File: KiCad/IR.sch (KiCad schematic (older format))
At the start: 30 parts, among them IC2 ATTINY85-P, IC3 ATTINY85-P, Q2 Q_NPN_BCE, Q3 Q_NPN_BCE

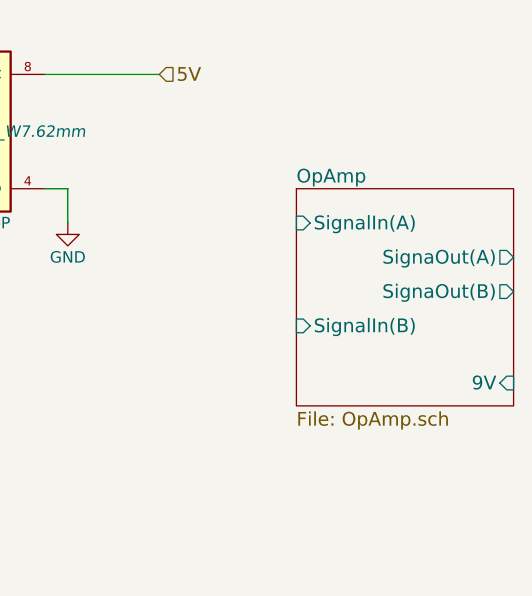
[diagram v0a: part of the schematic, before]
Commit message: Updated the schematics and started with the PCB
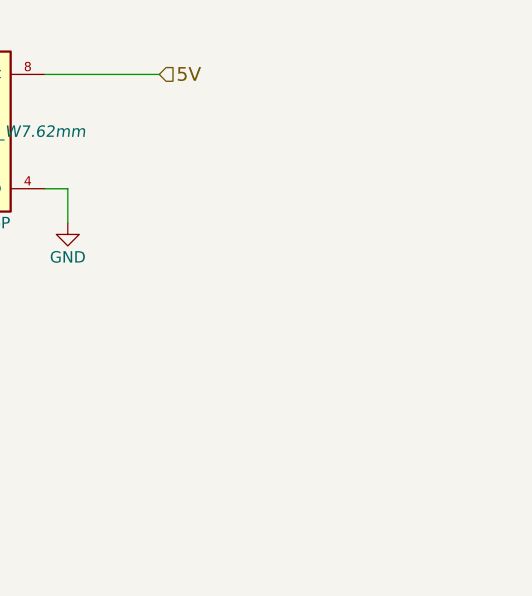
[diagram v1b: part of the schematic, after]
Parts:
- D1, D10, D11, D12, D2, D3, D4, D5, D6, D7, D8, D9: footprint LEDs:LED-5MM -> Wire_Connections_Bridges:WireConnection_1.50mmDrill
- R10, R11, R12, R13, R14, R15, R16, R17, R18, R19, R20, R21, R8, R9: footprint Resistors_ThroughHole:Resistor_Horizontal_RM20mm -> Resistors_ThroughHole:Resistor_Vertical_RM5mm
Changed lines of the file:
@@
 $Descr A4 11693 8268
 encoding utf-8
-Sheet 3 7
+Sheet 3 6
 Title ""
 Date ""
@@
 SCL
 $Comp
-L GND #PWR013
+L GND #PWR016
 U 1 1 57175BA8
 P 8550 2050
-F 0 "#PWR013" H 8550 1800 50  0001 C CNN
+F 0 "#PWR016" H 8550 1800 50  0001 C CNN
 F 1 "GND" H 8550 1900 50  0000 C CNN
 F 2 "" H 8550 2050 50  0000 C CNN
@@
 F 0 "D9" H 3200 3250 50  0000 C CNN
 F 1 "IR_Recieve" H 3216 2983 50  0000 C CNN
-F 2 "LEDs:LED-5MM" H 3200 3150 50  0001 C CNN
+F 2 "Wire_Connections_Bridges:WireConnection_1.50mmDrill" H 3200 3150 50  0001 C CNN
 F 3 "" H 3200 3150 50  0000 C CNN
 	1    3200 3150
@@
 F 0 "D7" H 2800 3250 50  0000 C CNN
 F 1 "LED" V 2800 3050 50  0000 C CNN
-F 2 "LEDs:LED-5MM" H 2800 3150 50  0001 C CNN
+F 2 "Wire_Connections_Bridges:WireConnection_1.50mmDrill" H 2800 3150 50  0001 C CNN
 F 3 "" H 2800 3150 50  0000 C CNN
 	1    2800 3150
@@
 F 0 "D11" H 3600 3250 50  0000 C CNN
 F 1 "LED" V 3600 3050 50  0000 C CNN
-F 2 "LEDs:LED-5MM" H 3600 3150 50  0001 C CNN
+F 2 "Wire_Connections_Bridges:WireConnection_1.50mmDrill" H 3600 3150 50  0001 C CNN
 F 3 "" H 3600 3150 50  0000 C CNN
 	1    3600 3150
@@
 F 0 "R16" V 3280 2600 50  0000 C CNN
 F 1 "100" V 3200 2600 50  0000 C CNN
-F 2 "Resistors_ThroughHole:Resistor_Horizontal_RM20mm" V 3130 2600 50  0001 C CNN
+F 2 "Resistors_ThroughHole:Resistor_Vertical_RM5mm" V 3130 2600 50  0001 C CNN
 F 3 "" H 3200 2600 50  0000 C CNN
 	1    3200 2600
@@
 F 0 "R18" V 3680 2600 50  0000 C CNN
 F 1 "22" V 3600 2600 50  0000 C CNN
-F 2 "Resistors_ThroughHole:Resistor_Horizontal_RM20mm" V 3530 2600 50  0001 C CNN
+F 2 "Resistors_ThroughHole:Resistor_Vertical_RM5mm" V 3530 2600 50  0001 C CNN
 F 3 "" H 3600 2600 50  0000 C CNN
 	1    3600 2600
@@
 F 0 "R14" V 2880 2600 50  0000 C CNN
 F 1 "22" V 2800 2600 50  0000 C CNN
-F 2 "Resistors_ThroughHole:Resistor_Horizontal_RM20mm" V 2730 2600 50  0001 C CNN
+F 2 "Resistors_ThroughHole:Resistor_Vertical_RM5mm" V 2730 2600 50  0001 C CNN
 F 3 "" H 2800 2600 50  0000 C CNN
 	1    2800 2600
@@
 F 0 "D3" H 1700 3250 50  0000 C CNN
 F 1 "IR_Recieve" H 1716 2983 50  0000 C CNN
-F 2 "LEDs:LED-5MM" H 1700 3150 50  0001 C CNN
+F 2 "Wire_Connections_Bridges:WireConnection_1.50mmDrill" H 1700 3150 50  0001 C CNN
 F 3 "" H 1700 3150 50  0000 C CNN
 	1    1700 3150
@@
 F 0 "D1" H 1300 3250 50  0000 C CNN
 F 1 "LED" V 1300 3050 50  0000 C CNN
-F 2 "LEDs:LED-5MM" H 1300 3150 50  0001 C CNN
+F 2 "Wire_Connections_Bridges:WireConnection_1.50mmDrill" H 1300 3150 50  0001 C CNN
 F 3 "" H 1300 3150 50  0000 C CNN
 	1    1300 3150
@@
 F 0 "D5" H 2100 3250 50  0000 C CNN
 F 1 "LED" V 2100 3050 50  0000 C CNN
-F 2 "LEDs:LED-5MM" H 2100 3150 50  0001 C CNN
+F 2 "Wire_Connections_Bridges:WireConnection_1.50mmDrill" H 2100 3150 50  0001 C CNN
 F 3 "" H 2100 3150 50  0000 C CNN
 	1    2100 3150
@@
 F 0 "R10" V 1780 2600 50  0000 C CNN
 F 1 "100" V 1700 2600 50  0000 C CNN
-F 2 "Resistors_ThroughHole:Resistor_Horizontal_RM20mm" V 1630 2600 50  0001 C CNN
+F 2 "Resistors_ThroughHole:Resistor_Vertical_RM5mm" V 1630 2600 50  0001 C CNN
 F 3 "" H 1700 2600 50  0000 C CNN
 	1    1700 2600
@@
 $EndComp
 $Comp
-L GND #PWR014
+L GND #PWR017
 U 1 1 57175C1F
 P 3900 3750
-F 0 "#PWR014" H 3900 3500 50  0001 C CNN
+F 0 "#PWR017" H 3900 3500 50  0001 C CNN
 F 1 "GND" H 3900 3600 50  0000 C CNN
 F 2 "" H 3900 3750 50  0000 C CNN
@@
 F 0 "R20" V 3880 4050 50  0000 C CNN
 F 1 "1K" V 3800 4050 50  0000 C CNN
-F 2 "Resistors_ThroughHole:Resistor_Horizontal_RM20mm" V 3730 4050 50  0001 C CNN
+F 2 "Resistors_ThroughHole:Resistor_Vertical_RM5mm" V 3730 4050 50  0001 C CNN
 F 3 "" H 3800 4050 50  0000 C CNN
 	1    3800 4050
@@
 F 0 "R12" V 2180 2600 50  0000 C CNN
 F 1 "22" V 2100 2600 50  0000 C CNN
-F 2 "Resistors_ThroughHole:Resistor_Horizontal_RM20mm" V 2030 2600 50  0001 C CNN
+F 2 "Resistors_ThroughHole:Resistor_Vertical_RM5mm" V 2030 2600 50  0001 C CNN
 F 3 "" H 2100 2600 50  0000 C CNN
 	1    2100 2600
@@
 F 0 "R8" V 1380 2600 50  0000 C CNN
 F 1 "22" V 1300 2600 50  0000 C CNN
-F 2 "Resistors_ThroughHole:Resistor_Horizontal_RM20mm" V 1230 2600 50  0001 C CNN
+F 2 "Resistors_ThroughHole:Resistor_Vertical_RM5mm" V 1230 2600 50  0001 C CNN
 F 3 "" H 1300 2600 50  0000 C CNN
 	1    1300 2600
@@
 SCL
 $Comp
-L GND #PWR015
+L GND #PWR018
 U 1 1 5718B310
 P 8550 5100
-F 0 "#PWR015" H 8550 4850 50  0001 C CNN
+F 0 "#PWR018" H 8550 4850 50  0001 C CNN
 F 1 "GND" H 8550 4950 50  0000 C CNN
 F 2 "" H 8550 5100 50  0000 C CNN
@@
 F 0 "D10" H 3200 6300 50  0000 C CNN
 F 1 "IR_Recieve" H 3216 6033 50  0000 C CNN
-F 2 "LEDs:LED-5MM" H 3200 6200 50  0001 C CNN
+F 2 "Wire_Connections_Bridges:WireConnection_1.50mmDrill" H 3200 6200 50  0001 C CNN
 F 3 "" H 3200 6200 50  0000 C CNN
 	1    3200 6200
@@
 F 0 "D8" H 2800 6300 50  0000 C CNN
 F 1 "LED" V 2800 6100 50  0000 C CNN
-F 2 "LEDs:LED-5MM" H 2800 6200 50  0001 C CNN
+F 2 "Wire_Connections_Bridges:WireConnection_1.50mmDrill" H 2800 6200 50  0001 C CNN
 F 3 "" H 2800 6200 50  0000 C CNN
 	1    2800 6200
@@
 F 0 "D12" H 3600 6300 50  0000 C CNN
 F 1 "LED" V 3600 6100 50  0000 C CNN
-F 2 "LEDs:LED-5MM" H 3600 6200 50  0001 C CNN
+F 2 "Wire_Connections_Bridges:WireConnection_1.50mmDrill" H 3600 6200 50  0001 C CNN
 F 3 "" H 3600 6200 50  0000 C CNN
 	1    3600 6200
@@
 F 0 "R17" V 3280 5650 50  0000 C CNN
 F 1 "100" V 3200 5650 50  0000 C CNN
-F 2 "Resistors_ThroughHole:Resistor_Horizontal_RM20mm" V 3130 5650 50  0001 C CNN
+F 2 "Resistors_ThroughHole:Resistor_Vertical_RM5mm" V 3130 5650 50  0001 C CNN
 F 3 "" H 3200 5650 50  0000 C CNN
 	1    3200 5650
@@
 F 0 "R19" V 3680 5650 50  0000 C CNN
 F 1 "22" V 3600 5650 50  0000 C CNN
-F 2 "Resistors_ThroughHole:Resistor_Horizontal_RM20mm" V 3530 5650 50  0001 C CNN
+F 2 "Resistors_ThroughHole:Resistor_Vertical_RM5mm" V 3530 5650 50  0001 C CNN
 F 3 "" H 3600 5650 50  0000 C CNN
 	1    3600 5650
@@
 F 0 "R15" V 2880 5650 50  0000 C CNN
 F 1 "22" V 2800 5650 50  0000 C CNN
-F 2 "Resistors_ThroughHole:Resistor_Horizontal_RM20mm" V 2730 5650 50  0001 C CNN
+F 2 "Resistors_ThroughHole:Resistor_Vertical_RM5mm" V 2730 5650 50  0001 C CNN
 F 3 "" H 2800 5650 50  0000 C CNN
 	1    2800 5650
@@
 F 0 "D4" H 1700 6300 50  0000 C CNN
 F 1 "IR_Recieve" H 1716 6033 50  0000 C CNN
-F 2 "LEDs:LED-5MM" H 1700 6200 50  0001 C CNN
+F 2 "Wire_Connections_Bridges:WireConnection_1.50mmDrill" H 1700 6200 50  0001 C CNN
 F 3 "" H 1700 6200 50  0000 C CNN
 	1    1700 6200
@@
 F 0 "D2" H 1300 6300 50  0000 C CNN
 F 1 "LED" V 1300 6100 50  0000 C CNN
-F 2 "LEDs:LED-5MM" H 1300 6200 50  0001 C CNN
+F 2 "Wire_Connections_Bridges:WireConnection_1.50mmDrill" H 1300 6200 50  0001 C CNN
 F 3 "" H 1300 6200 50  0000 C CNN
 	1    1300 6200
@@
 F 0 "D6" H 2100 6300 50  0000 C CNN
 F 1 "LED" V 2100 6100 50  0000 C CNN
-F 2 "LEDs:LED-5MM" H 2100 6200 50  0001 C CNN
+F 2 "Wire_Connections_Bridges:WireConnection_1.50mmDrill" H 2100 6200 50  0001 C CNN
 F 3 "" H 2100 6200 50  0000 C CNN
 	1    2100 6200
@@
 F 0 "R11" V 1780 5650 50  0000 C CNN
 F 1 "100" V 1700 5650 50  0000 C CNN
-F 2 "Resistors_ThroughHole:Resistor_Horizontal_RM20mm" V 1630 5650 50  0001 C CNN
+F 2 "Resistors_ThroughHole:Resistor_Vertical_RM5mm" V 1630 5650 50  0001 C CNN
 F 3 "" H 1700 5650 50  0000 C CNN
 	1    1700 5650
@@
 $EndComp
 $Comp
-L GND #PWR016
+L GND #PWR019
 U 1 1 5718B359
 P 3900 6800
-F 0 "#PWR016" H 3900 6550 50  0001 C CNN
+F 0 "#PWR019" H 3900 6550 50  0001 C CNN
 F 1 "GND" H 3900 6650 50  0000 C CNN
 F 2 "" H 3900 6800 50  0000 C CNN
@@
 F 0 "R21" V 3880 7100 50  0000 C CNN
 F 1 "1K" V 3800 7100 50  0000 C CNN
-F 2 "Resistors_ThroughHole:Resistor_Horizontal_RM20mm" V 3730 7100 50  0001 C CNN
+F 2 "Resistors_ThroughHole:Resistor_Vertical_RM5mm" V 3730 7100 50  0001 C CNN
 F 3 "" H 3800 7100 50  0000 C CNN
 	1    3800 7100
@@
 F 0 "R13" V 2180 5650 50  0000 C CNN
 F 1 "22" V 2100 5650 50  0000 C CNN
-F 2 "Resistors_ThroughHole:Resistor_Horizontal_RM20mm" V 2030 5650 50  0001 C CNN
+F 2 "Resistors_ThroughHole:Resistor_Vertical_RM5mm" V 2030 5650 50  0001 C CNN
 F 3 "" H 2100 5650 50  0000 C CNN
 	1    2100 5650
@@
 F 0 "R9" V 1380 5650 50  0000 C CNN
 F 1 "22" V 1300 5650 50  0000 C CNN
-F 2 "Resistors_ThroughHole:Resistor_Horizontal_RM20mm" V 1230 5650 50  0001 C CNN
+F 2 "Resistors_ThroughHole:Resistor_Vertical_RM5mm" V 1230 5650 50  0001 C CNN
 F 3 "" H 1300 5650 50  0000 C CNN
 	1    1300 5650
@@
 Text HLabel 3600 5500 1    60   Input ~ 0
 3V
-$Sheet
-S 9550 4950 950  950
-U 5718B39F
-F0 "OpAmp" 60
-F1 "OpAmp.sch" 60
-F2 "SignalIn(A)" I L 9550 5100 60
-F3 "SignaOut(A)" O R 10500 5250 60
-F4 "9V" I R 10500 5800 60
-F5 "SignaOut(B)" O R 10500 5400 60
-F6 "SignalIn(B)" I L 9550 5550 60
-$EndSheet
 Wire Wire Line
 	8950 1400 8450 1400

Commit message: Started with the PCB
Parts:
- removed Q3: Q_NPN_BCE, TO_SOT_Packages_THT:TO-92_Inline_Narrow_Oval, symbol Q_NPN_BCE
- removed R21: 1K, Resistors_ThroughHole:Resistor_Vertical_RM5mm, symbol R
- added P3, P4: CONN_01X02, Pin_Headers:Pin_Header_Straight_2x01, symbol CONN_01X02
- added P5: CONN_02X04, Pin_Headers:Pin_Header_Straight_2x04, symbol CONN_02X04
- added P6: CONN_02X03, Pin_Headers:Pin_Header_Straight_2x03, symbol CONN_02X03
- added Q1: Q_NPN_BCE, TO_SOT_Packages_THT:TO-92_Inline_Narrow_Oval, symbol Q_NPN_BCE
- added R4: 22, Resistors_ThroughHole:Resistor_Vertical_RM5mm, symbol R
- R11, R17: value 100 -> 22
- R15, R9: value 22 -> 100
- R19: value 22 -> 1K
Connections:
- net 3V: now also R11.1, R17.1, R4.1; no longer R15.1, R19.1, R9.1
- net 5V: now also R15.1, R9.1; no longer R11.1, R17.1
- net GND: now also P6.4 (P4), Q1.3 (E)
- net SCL: now also P3.1 (P1), P4.1 (P1); no longer IC2.7 (PB2(SCK/USCK/SCL/T0/INT0/ADC1/PCINT2)), IC3.7 (PB2(SCK/USCK/SCL/T0/INT0/ADC1/PCINT2))
- net SDA: now also P5.1 (P1), P5.3 (P3)
- net Signal: now also R15.2, R9.2; no longer R11.2, R17.2
- net at IC2.1 (PB5(~RESET~/dW/ADC0/PCINT5)), R20.1: now also IC3.1 (PB5(~RESET~/dW/ADC0/PCINT5)), R19.1, P6.6 (P6)
- net at IC2.6 (PB1(MISO/DO/AIN1/OC0B/OC1A/PCINT1)): now also P5.5 (P5)
- net at IC3.6 (PB1(MISO/DO/AIN1/OC0B/OC1A/PCINT1)): now also P5.7 (P7)
- net at D10.1 (K), D12.1 (K), D2.1 (K)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: now also Q1.2 (C)
- net at D8.2 (A): now also R13.2; no longer R15.2
- net at D12.2 (A): now also R17.2; no longer R19.2
- net at D2.2 (A): now also R4.2; no longer R9.2
- net at D6.2 (A): now also R11.2; no longer R13.2
- new net: IC2.7 (PB2(SCK/USCK/SCL/T0/INT0/ADC1/PCINT2)), IC3.7 (PB2(SCK/USCK/SCL/T0/INT0/ADC1/PCINT2)), P3.2 (P2), P4.2 (P2), P6.5 (P5)
- new net: Q1.1 (B), R19.2
- new net: P5.2 (P2), P5.4 (P4), P6.1 (P1)
- new net: P5.6 (P6), P5.8 (P8), P6.3 (P3)
- no-connect marks 0 -> 1
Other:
- moved on the sheet: D1, D11, D3, D5, D7, D9, IC2, Q2, R10, R12, R14, R16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

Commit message: Added smaller footprints
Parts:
- D1, D10, D11, D12, D2, D3, D4, D5, D6, D7, D8, D9: footprint Wire_Connections_Bridges:WireConnection_1.50mmDrill -> Wire_Pads:SolderWirePad_2x_1mmDrill
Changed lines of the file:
@@
 SCL
 $Comp
-L GND #PWR17
+L GND #PWR015
 U 1 1 57175BA8
 P 8650 1700
-F 0 "#PWR17" H 8650 1450 50  0001 C CNN
+F 0 "#PWR015" H 8650 1450 50  0001 C CNN
 F 1 "GND" H 8650 1550 50  0000 C CNN
 F 2 "" H 8650 1700 50  0000 C CNN
@@
 F 0 "D9" H 3300 2900 50  0000 C CNN
 F 1 "IR_Recieve" H 3316 2633 50  0000 C CNN
-F 2 "Wire_Connections_Bridges:WireConnection_1.50mmDrill" H 3300 2800 50  0001 C CNN
+F 2 "Wire_Pads:SolderWirePad_2x_1mmDrill" H 3300 2800 50  0001 C CNN
 F 3 "" H 3300 2800 50  0000 C CNN
 	1    3300 2800
@@
 F 0 "D7" H 2900 2900 50  0000 C CNN
 F 1 "LED" V 2900 2700 50  0000 C CNN
-F 2 "Wire_Connections_Bridges:WireConnection_1.50mmDrill" H 2900 2800 50  0001 C CNN
+F 2 "Wire_Pads:SolderWirePad_2x_1mmDrill" H 2900 2800 50  0001 C CNN
 F 3 "" H 2900 2800 50  0000 C CNN
 	1    2900 2800
@@
 F 0 "D11" H 3700 2900 50  0000 C CNN
 F 1 "LED" V 3700 2700 50  0000 C CNN
-F 2 "Wire_Connections_Bridges:WireConnection_1.50mmDrill" H 3700 2800 50  0001 C CNN
+F 2 "Wire_Pads:SolderWirePad_2x_1mmDrill" H 3700 2800 50  0001 C CNN
 F 3 "" H 3700 2800 50  0000 C CNN
 	1    3700 2800
@@
 F 0 "D3" H 1800 2900 50  0000 C CNN
 F 1 "IR_Recieve" H 1816 2633 50  0000 C CNN
-F 2 "Wire_Connections_Bridges:WireConnection_1.50mmDrill" H 1800 2800 50  0001 C CNN
+F 2 "Wire_Pads:SolderWirePad_2x_1mmDrill" H 1800 2800 50  0001 C CNN
 F 3 "" H 1800 2800 50  0000 C CNN
 	1    1800 2800
@@
 F 0 "D1" H 1400 2900 50  0000 C CNN
 F 1 "LED" V 1400 2700 50  0000 C CNN
-F 2 "Wire_Connections_Bridges:WireConnection_1.50mmDrill" H 1400 2800 50  0001 C CNN
+F 2 "Wire_Pads:SolderWirePad_2x_1mmDrill" H 1400 2800 50  0001 C CNN
 F 3 "" H 1400 2800 50  0000 C CNN
 	1    1400 2800
@@
 F 0 "D5" H 2200 2900 50  0000 C CNN
 F 1 "LED" V 2200 2700 50  0000 C CNN
-F 2 "Wire_Connections_Bridges:WireConnection_1.50mmDrill" H 2200 2800 50  0001 C CNN
+F 2 "Wire_Pads:SolderWirePad_2x_1mmDrill" H 2200 2800 50  0001 C CNN
 F 3 "" H 2200 2800 50  0000 C CNN
 	1    2200 2800
@@
 $EndComp
 $Comp
-L GND #PWR15
+L GND #PWR016
 U 1 1 57175C1F
 P 4000 3400
-F 0 "#PWR15" H 4000 3150 50  0001 C CNN
+F 0 "#PWR016" H 4000 3150 50  0001 C CNN
 F 1 "GND" H 4000 3250 50  0000 C CNN
 F 2 "" H 4000 3400 50  0000 C CNN
@@
 SCL
 $Comp
-L GND #PWR18
+L GND #PWR017
 U 1 1 5735BAD5
 P 8700 5100
-F 0 "#PWR18" H 8700 4850 50  0001 C CNN
+F 0 "#PWR017" H 8700 4850 50  0001 C CNN
 F 1 "GND" H 8700 4950 50  0000 C CNN
 F 2 "" H 8700 5100 50  0000 C CNN
@@
 F 0 "D10" H 3350 6300 50  0000 C CNN
 F 1 "IR_Recieve" H 3366 6033 50  0000 C CNN
-F 2 "Wire_Connections_Bridges:WireConnection_1.50mmDrill" H 3350 6200 50  0001 C CNN
+F 2 "Wire_Pads:SolderWirePad_2x_1mmDrill" H 3350 6200 50  0001 C CNN
 F 3 "" H 3350 6200 50  0000 C CNN
 	1    3350 6200
@@
 F 0 "D8" H 2950 6300 50  0000 C CNN
 F 1 "LED" V 2950 6100 50  0000 C CNN
-F 2 "Wire_Connections_Bridges:WireConnection_1.50mmDrill" H 2950 6200 50  0001 C CNN
+F 2 "Wire_Pads:SolderWirePad_2x_1mmDrill" H 2950 6200 50  0001 C CNN
 F 3 "" H 2950 6200 50  0000 C CNN
 	1    2950 6200
@@
 F 0 "D12" H 3750 6300 50  0000 C CNN
 F 1 "LED" V 3750 6100 50  0000 C CNN
-F 2 "Wire_Connections_Bridges:WireConnection_1.50mmDrill" H 3750 6200 50  0001 C CNN
+F 2 "Wire_Pads:SolderWirePad_2x_1mmDrill" H 3750 6200 50  0001 C CNN
 F 3 "" H 3750 6200 50  0000 C CNN
 	1    3750 6200
@@
 F 0 "D4" H 1850 6300 50  0000 C CNN
 F 1 "IR_Recieve" H 1866 6033 50  0000 C CNN
-F 2 "Wire_Connections_Bridges:WireConnection_1.50mmDrill" H 1850 6200 50  0001 C CNN
+F 2 "Wire_Pads:SolderWirePad_2x_1mmDrill" H 1850 6200 50  0001 C CNN
 F 3 "" H 1850 6200 50  0000 C CNN
 	1    1850 6200
@@
 F 0 "D2" H 1450 6300 50  0000 C CNN
 F 1 "LED" V 1450 6100 50  0000 C CNN
-F 2 "Wire_Connections_Bridges:WireConnection_1.50mmDrill" H 1450 6200 50  0001 C CNN
+F 2 "Wire_Pads:SolderWirePad_2x_1mmDrill" H 1450 6200 50  0001 C CNN
 F 3 "" H 1450 6200 50  0000 C CNN
 	1    1450 6200
@@
 F 0 "D6" H 2250 6300 50  0000 C CNN
 F 1 "LED" V 2250 6100 50  0000 C CNN
-F 2 "Wire_Connections_Bridges:WireConnection_1.50mmDrill" H 2250 6200 50  0001 C CNN
+F 2 "Wire_Pads:SolderWirePad_2x_1mmDrill" H 2250 6200 50  0001 C CNN
 F 3 "" H 2250 6200 50  0000 C CNN
 	1    2250 6200
@@
 $EndComp
 $Comp
-L GND #PWR16
+L GND #PWR018
 U 1 1 5735BB1E
 P 4050 6800
-F 0 "#PWR16" H 4050 6550 50  0001 C CNN
+F 0 "#PWR018" H 4050 6550 50  0001 C CNN
 F 1 "GND" H 4050 6650 50  0000 C CNN
 F 2 "" H 4050 6800 50  0000 C CNN
@@
 Connection ~ 9300 3850
 $Comp
-L GND #PWR19
+L GND #PWR019
 U 1 1 5735C5A5
 P 9300 2950
-F 0 "#PWR19" H 9300 2700 50  0001 C CNN
+F 0 "#PWR019" H 9300 2700 50  0001 C CNN
 F 1 "GND" H 9300 2800 50  0000 C CNN
 F 2 "" H 9300 2950 50  0000 C CNN

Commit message: Revert "Added smaller footprints"
This reverts commit 0613a684753a289cb87120d105616d3a60c555f9.
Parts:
- D1, D10, D11, D12, D2, D3, D4, D5, D6, D7, D8, D9: footprint Wire_Pads:SolderWirePad_2x_1mmDrill -> Wire_Connections_Bridges:WireConnection_1.50mmDrill
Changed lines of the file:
@@
 SCL
 $Comp
-L GND #PWR015
+L GND #PWR17
 U 1 1 57175BA8
 P 8650 1700
-F 0 "#PWR015" H 8650 1450 50  0001 C CNN
+F 0 "#PWR17" H 8650 1450 50  0001 C CNN
 F 1 "GND" H 8650 1550 50  0000 C CNN
 F 2 "" H 8650 1700 50  0000 C CNN
@@
 F 0 "D9" H 3300 2900 50  0000 C CNN
 F 1 "IR_Recieve" H 3316 2633 50  0000 C CNN
-F 2 "Wire_Pads:SolderWirePad_2x_1mmDrill" H 3300 2800 50  0001 C CNN
+F 2 "Wire_Connections_Bridges:WireConnection_1.50mmDrill" H 3300 2800 50  0001 C CNN
 F 3 "" H 3300 2800 50  0000 C CNN
 	1    3300 2800
@@
 F 0 "D7" H 2900 2900 50  0000 C CNN
 F 1 "LED" V 2900 2700 50  0000 C CNN
-F 2 "Wire_Pads:SolderWirePad_2x_1mmDrill" H 2900 2800 50  0001 C CNN
+F 2 "Wire_Connections_Bridges:WireConnection_1.50mmDrill" H 2900 2800 50  0001 C CNN
 F 3 "" H 2900 2800 50  0000 C CNN
 	1    2900 2800
@@
 F 0 "D11" H 3700 2900 50  0000 C CNN
 F 1 "LED" V 3700 2700 50  0000 C CNN
-F 2 "Wire_Pads:SolderWirePad_2x_1mmDrill" H 3700 2800 50  0001 C CNN
+F 2 "Wire_Connections_Bridges:WireConnection_1.50mmDrill" H 3700 2800 50  0001 C CNN
 F 3 "" H 3700 2800 50  0000 C CNN
 	1    3700 2800
@@
 F 0 "D3" H 1800 2900 50  0000 C CNN
 F 1 "IR_Recieve" H 1816 2633 50  0000 C CNN
-F 2 "Wire_Pads:SolderWirePad_2x_1mmDrill" H 1800 2800 50  0001 C CNN
+F 2 "Wire_Connections_Bridges:WireConnection_1.50mmDrill" H 1800 2800 50  0001 C CNN
 F 3 "" H 1800 2800 50  0000 C CNN
 	1    1800 2800
@@
 F 0 "D1" H 1400 2900 50  0000 C CNN
 F 1 "LED" V 1400 2700 50  0000 C CNN
-F 2 "Wire_Pads:SolderWirePad_2x_1mmDrill" H 1400 2800 50  0001 C CNN
+F 2 "Wire_Connections_Bridges:WireConnection_1.50mmDrill" H 1400 2800 50  0001 C CNN
 F 3 "" H 1400 2800 50  0000 C CNN
 	1    1400 2800
@@
 F 0 "D5" H 2200 2900 50  0000 C CNN
 F 1 "LED" V 2200 2700 50  0000 C CNN
-F 2 "Wire_Pads:SolderWirePad_2x_1mmDrill" H 2200 2800 50  0001 C CNN
+F 2 "Wire_Connections_Bridges:WireConnection_1.50mmDrill" H 2200 2800 50  0001 C CNN
 F 3 "" H 2200 2800 50  0000 C CNN
 	1    2200 2800
@@
 $EndComp
 $Comp
-L GND #PWR016
+L GND #PWR15
 U 1 1 57175C1F
 P 4000 3400
-F 0 "#PWR016" H 4000 3150 50  0001 C CNN
+F 0 "#PWR15" H 4000 3150 50  0001 C CNN
 F 1 "GND" H 4000 3250 50  0000 C CNN
 F 2 "" H 4000 3400 50  0000 C CNN
@@
 SCL
 $Comp
-L GND #PWR017
+L GND #PWR18
 U 1 1 5735BAD5
 P 8700 5100
-F 0 "#PWR017" H 8700 4850 50  0001 C CNN
+F 0 "#PWR18" H 8700 4850 50  0001 C CNN
 F 1 "GND" H 8700 4950 50  0000 C CNN
 F 2 "" H 8700 5100 50  0000 C CNN
@@
 F 0 "D10" H 3350 6300 50  0000 C CNN
 F 1 "IR_Recieve" H 3366 6033 50  0000 C CNN
-F 2 "Wire_Pads:SolderWirePad_2x_1mmDrill" H 3350 6200 50  0001 C CNN
+F 2 "Wire_Connections_Bridges:WireConnection_1.50mmDrill" H 3350 6200 50  0001 C CNN
 F 3 "" H 3350 6200 50  0000 C CNN
 	1    3350 6200
@@
 F 0 "D8" H 2950 6300 50  0000 C CNN
 F 1 "LED" V 2950 6100 50  0000 C CNN
-F 2 "Wire_Pads:SolderWirePad_2x_1mmDrill" H 2950 6200 50  0001 C CNN
+F 2 "Wire_Connections_Bridges:WireConnection_1.50mmDrill" H 2950 6200 50  0001 C CNN
 F 3 "" H 2950 6200 50  0000 C CNN
 	1    2950 6200
@@
 F 0 "D12" H 3750 6300 50  0000 C CNN
 F 1 "LED" V 3750 6100 50  0000 C CNN
-F 2 "Wire_Pads:SolderWirePad_2x_1mmDrill" H 3750 6200 50  0001 C CNN
+F 2 "Wire_Connections_Bridges:WireConnection_1.50mmDrill" H 3750 6200 50  0001 C CNN
 F 3 "" H 3750 6200 50  0000 C CNN
 	1    3750 6200
@@
 F 0 "D4" H 1850 6300 50  0000 C CNN
 F 1 "IR_Recieve" H 1866 6033 50  0000 C CNN
-F 2 "Wire_Pads:SolderWirePad_2x_1mmDrill" H 1850 6200 50  0001 C CNN
+F 2 "Wire_Connections_Bridges:WireConnection_1.50mmDrill" H 1850 6200 50  0001 C CNN
 F 3 "" H 1850 6200 50  0000 C CNN
 	1    1850 6200
@@
 F 0 "D2" H 1450 6300 50  0000 C CNN
 F 1 "LED" V 1450 6100 50  0000 C CNN
-F 2 "Wire_Pads:SolderWirePad_2x_1mmDrill" H 1450 6200 50  0001 C CNN
+F 2 "Wire_Connections_Bridges:WireConnection_1.50mmDrill" H 1450 6200 50  0001 C CNN
 F 3 "" H 1450 6200 50  0000 C CNN
 	1    1450 6200
@@
 F 0 "D6" H 2250 6300 50  0000 C CNN
 F 1 "LED" V 2250 6100 50  0000 C CNN
-F 2 "Wire_Pads:SolderWirePad_2x_1mmDrill" H 2250 6200 50  0001 C CNN
+F 2 "Wire_Connections_Bridges:WireConnection_1.50mmDrill" H 2250 6200 50  0001 C CNN
 F 3 "" H 2250 6200 50  0000 C CNN
 	1    2250 6200
@@
 $EndComp
 $Comp
-L GND #PWR018
+L GND #PWR16
 U 1 1 5735BB1E
 P 4050 6800
-F 0 "#PWR018" H 4050 6550 50  0001 C CNN
+F 0 "#PWR16" H 4050 6550 50  0001 C CNN
 F 1 "GND" H 4050 6650 50  0000 C CNN
 F 2 "" H 4050 6800 50  0000 C CNN
@@
 Connection ~ 9300 3850
 $Comp
-L GND #PWR019
+L GND #PWR19
 U 1 1 5735C5A5
 P 9300 2950
-F 0 "#PWR019" H 9300 2700 50  0001 C CNN
+F 0 "#PWR19" H 9300 2700 50  0001 C CNN
 F 1 "GND" H 9300 2800 50  0000 C CNN
 F 2 "" H 9300 2950 50  0000 C CNN
